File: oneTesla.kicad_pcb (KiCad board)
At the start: 2 copper layers, 100 x 100 mm, 45 parts, among them IC1 74HCT14, IC2 74HCT74, IC3 UCC37321P, IC4 UCC37321P, IC6 MC7805BDTRKG, J1 2EDGRC-5.08-02P, J110 Jumper 110V, P1 PRIMARIO A, P2 PRIMARIO B, Q1 FGA60N65SMD, Q2 FGA60N65SMD, T1 1:1:1, T3 1:300

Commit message: Atualiza footprints dos capacitores e aterramento M3 do controle
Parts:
- removed the REF** at (37.4, 121.0)
- added J2: PE / GND CONTROLE, oneTesla:PE_GND_Control_M3_D7.0mm, F.Cu at (37.4, 121.0)
- C11, C12: footprint oneTesla:CP_D25_H45_P10.16_ReviewPending -> oneTesla:CP_SnapIn_D30.3_H40.5_P10.00_ReviewPending
- moved R5 12.9 mm to (84.8, 50.8)
- moved R6 10.7 mm to (115.5, 50.8)
- moved Z1 10.3 mm to (120.2, 85.2), turned to 180 degrees
- moved D4 9.91 mm to (63.5, 62.0)
- moved PS1 9.05 mm to (49.6, 30.9)
- moved Z2 8.75 mm to (120.2, 92.5), turned to 0 degrees
- moved F1 7.90 mm to (77.0, 35.0)
- moved C12 7.25 mm to (84.5, 56.0)
- moved J110 4.25 mm to (100.2, 37.8)
- moved C11 2.25 mm to (115.5, 56.0)
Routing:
- net GND: track 20.8 -> 35.6 mm
- net /AC_N: track 107.0 -> 114.7 mm
- net /AC_L: track 18.6 -> 25.5 mm
- net +15V: track 81.8 -> 75.8 mm
- net /SW_NODE: track 94.3 -> 95.7 mm
- net Net-(D1-K): track 44.9 -> 43.5 mm
- net /DC_PLUS: track 6.46 -> 5.30 mm

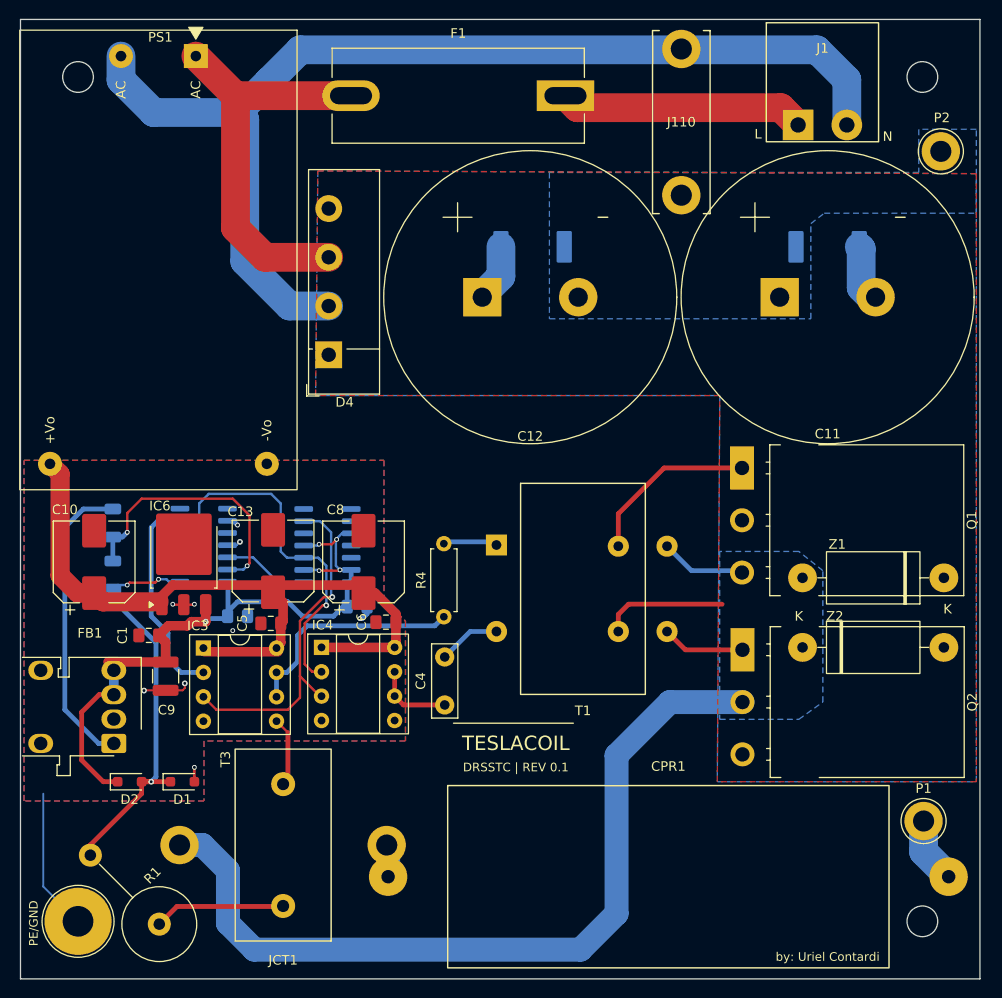
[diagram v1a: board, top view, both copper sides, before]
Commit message: Atualiza PCB e arquivos de produção com revisão final
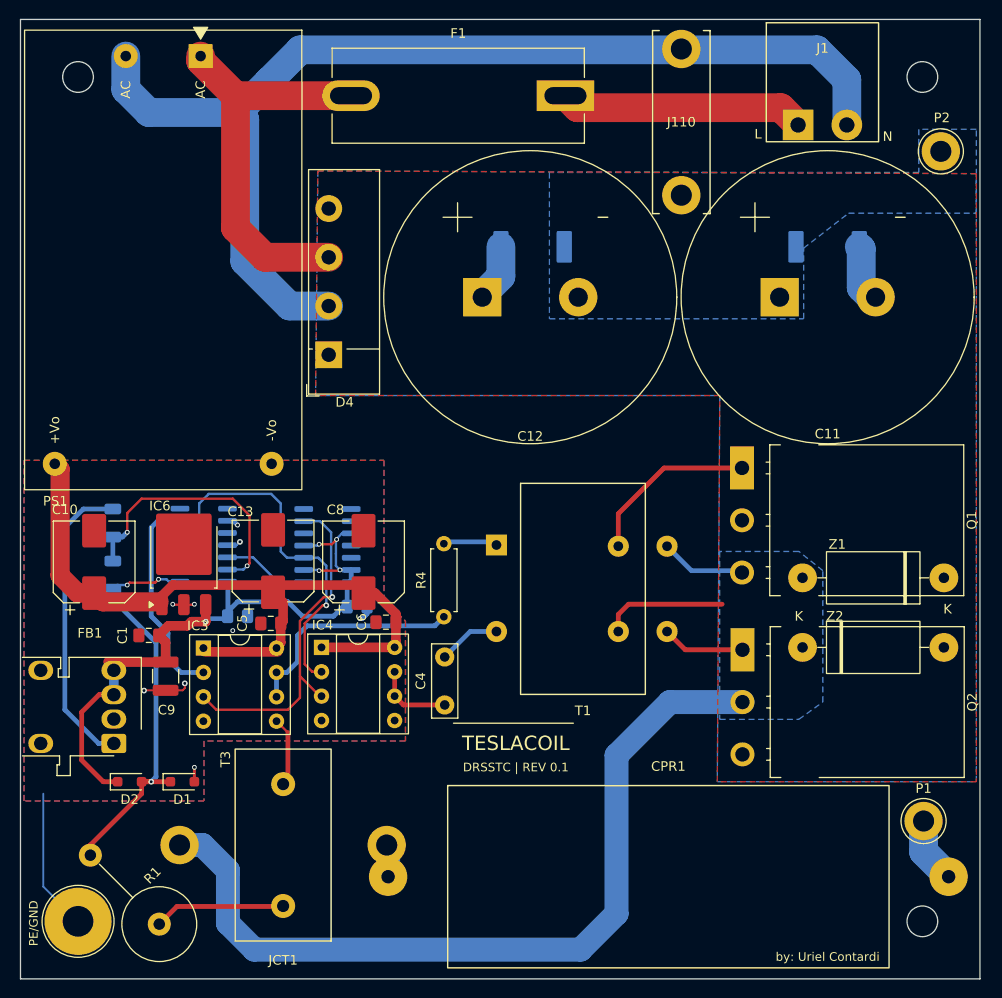
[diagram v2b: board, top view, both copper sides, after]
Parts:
- moved PS1 0.50 mm to (50.1, 30.9)

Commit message: Salva revisão DFM, arquivos de fabricação e modelos 3D completos
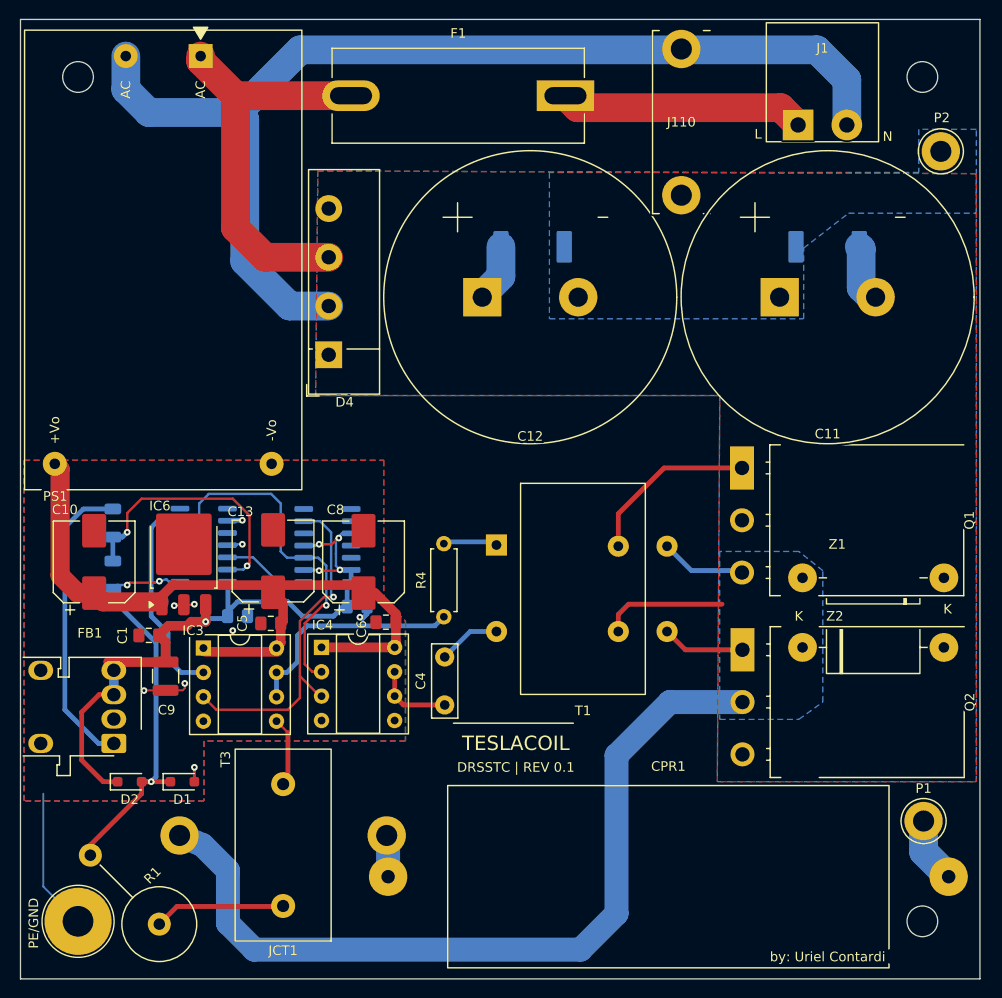
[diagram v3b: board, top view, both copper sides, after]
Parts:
- C12: footprint oneTesla:CP_SnapIn_D30.3_H40.5_P10.00_ReviewPending -> oneTesla:CP_SnapIn_D30.3_H40.5_P10.00_ReviewPending_DFM_C12
- C13: footprint oneTesla:CP_Elec_8x10 -> oneTesla:CP_Elec_8x10_DFM_C13
- C2: footprint oneTesla:C_0805_2012Metric_Pad1.18x1.45mm_HandSolder -> oneTesla:C_0805_2012Metric_Pad1.18x1.45mm_HandSolder_DFM_C2
- C8: footprint oneTesla:CP_Elec_8x10 -> oneTesla:CP_Elec_8x10_DFM_C8
- CPR1: footprint oneTesla:CDE_940C30S68K_F_CONFIRMAR -> oneTesla:CDE_940C30S68K_F_CONFIRMAR_DFM_CPR1
- D4: footprint oneTesla:Diode_Bridge_Vishay_KBU -> oneTesla:Diode_Bridge_Vishay_KBU_DFM_D4
- FB1: footprint oneTesla:HFBR-2521ETZ -> oneTesla:HFBR-2521ETZ_DFM_FB1
- IC3: footprint oneTesla:DIP-8_W7.62mm_Socket_LongPads -> oneTesla:DIP-8_W7.62mm_Socket_LongPads_DFM_IC3
- IC4: footprint oneTesla:DIP-8_W7.62mm_Socket_LongPads -> oneTesla:DIP-8_W7.62mm_Socket_LongPads_DFM_IC4
- J1: footprint oneTesla:TerminalBlock_2EDGRC-5.08_1x02_P5.08mm_Horizontal -> oneTesla:TerminalBlock_2EDGRC-5.08_1x02_P5.08mm_Horizontal_DFM_J1
- J110: footprint oneTesla:J110_WireLink_P15.24mm -> oneTesla:J110_WireLink_P15.24mm_DFM_J110
- J2: footprint oneTesla:PE_GND_Control_M3_D7.0mm -> oneTesla:PE_GND_Control_M3_D7.0mm_DFM_J2
- PS1: footprint oneTesla:HLK-15M15BL -> oneTesla:HLK-15M15BL_DFM_PS1
- Q1: footprint oneTesla:Q_TO3P_ImportedPads_ReviewPending -> oneTesla:Q_TO3P_ImportedPads_ReviewPending_DFM_Q1
- Q2: footprint oneTesla:Q_TO3P_ImportedPads_ReviewPending -> oneTesla:Q_TO3P_ImportedPads_ReviewPending_DFM_Q2
- R1: footprint oneTesla:R_Axial_Vishay_AC05_L18.0mm_D7.5mm_P10.16mm_Vertical -> oneTesla:R_Axial_Vishay_AC05_L18.0mm_D7.5mm_P10.16mm_Vertical_DFM_R1
- Z1: footprint oneTesla:D_DO201AD_P14.732_ReviewPending -> oneTesla:D_DO201AD_P14.732_ReviewPending_DFM_Z1
- Z2: footprint oneTesla:D_DO201AD_P14.732_ReviewPending -> oneTesla:D_DO201AD_P14.732_ReviewPending_DFM_Z2
- moved JCT1 1.00 mm to (58.8, 112.1)
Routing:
- net /SW_CT: track 3.36 -> 4.31 mm
- net GND: track 35.6 -> 36.2 mm
